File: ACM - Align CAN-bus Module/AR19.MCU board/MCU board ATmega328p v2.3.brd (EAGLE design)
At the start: 25.4 x 39 mm, 40 parts, among them IC1 ATMEGA328P-MMH, IC2 MIC5239-5.0YS_TR, IC3 MCP25625-E_ML, J1 AVR_SPI_PROG_3X2NS

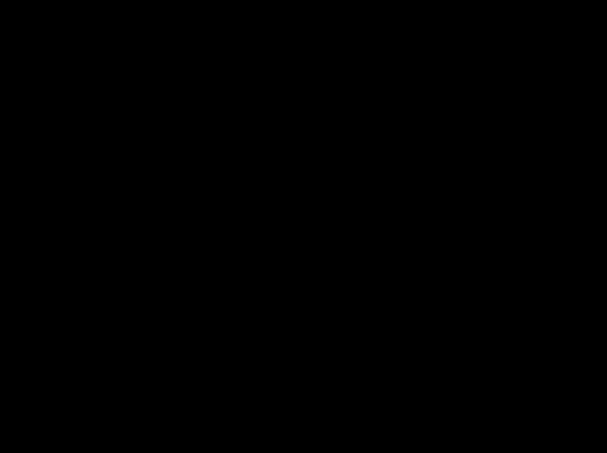
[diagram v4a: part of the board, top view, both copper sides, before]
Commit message: Added: Orange Power LED with 500ohm resistor
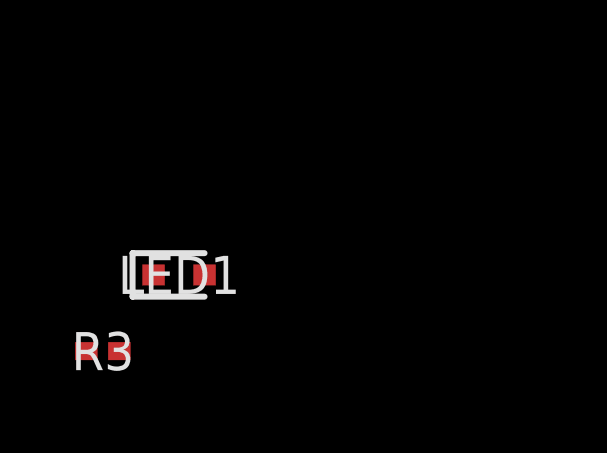
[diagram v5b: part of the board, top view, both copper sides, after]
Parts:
- added LED1: SML-A12DTT86, SML-A12DTT86:LEDC1606X125N
- added R3: 500Ohm, CRCW040295R3FKED(0402):RESC1005X40N
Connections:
- new net N$3: LED1.1, R3.1
- net GND: now also LED1.2
- net N$2: now also R3.2
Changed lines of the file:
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@@
 <attribute name="VALUE" x="10.6813" y="53.728" size="1.27" layer="27" align="center"/>
+</element>
+<element name="LED1" library="SML-A12DTT86" package="LEDC1606X125N" value="SML-A12DTT86" x="-34.29" y="-59.69" smashed="yes">
+<attribute name="ALLIED_NUMBER" value="70522054" x="-34.29" y="-59.69" size="1.778" layer="27" display="off"/>
+<attribute name="ALLIED_PRICE-STOCK" value="https://www.alliedelec.com/rohm-semiconductor-sml-a12dtt86/70522054/" x="-34.29" y="-59.69" size="1.778" layer="27" display="off"/>
+<attribute name="ARROW_PART_NUMBER" value="SML-A12DTT86" x="-34.29" y="-59.69" size="1.778" layer="27" display="off"/>
+<attribute name="ARROW_PRICE-STOCK" value="http://uk.rs-online.com/web/p/products/7008008P" x="-34.29" y="-59.69" size="1.778" layer="27" display="off"/>
+<attribute name="DESCRIPTION" value="Mini-mold side view chip LED : ROHM's chip LED lineup consists of standard type,top-view type, side-view type and reverse-mount type." x="-34.29" y="-59.69" size="1.778" layer="27" display="off"/>
+<attribute name="HEIGHT" value="1.25mm" x="-34.29" y="-59.69" size="1.778" layer="27" display="off"/>
+<attribute name="MANUFACTURER_NAME" value="ROHM Semiconductor" x="-34.29" y="-59.69" size="1.778" layer="27" display="off"/>
+<attribute name="MANUFACTURER_PART_NUMBER" value="SML-A12DTT86" x="-34.29" y="-59.69" size="1.778" layer="27" display="off"/>
+<attribute name="NAME" x="-34.29" y="-59.69" size="1.27" layer="25" align="center"/>
+<attribute name="RS_PART_NUMBER" value="7008008P" x="-34.29" y="-59.69" size="1.778" layer="27" display="off"/>
+<attribute name="RS_PRICE-STOCK" value="http://uk.rs-online.com/web/p/products/7008008P" x="-34.29" y="-59.69" size="1.778" layer="27" display="off"/>
+<attribute name="VALUE" x="-34.29" y="-59.69" size="1.27" layer="27" align="center"/>
+</element>
+<element name="R3" library="CRCW040295R3FKED(0402)" package="RESC1005X40N" value="500Ohm" x="-36.83" y="-62.23" smashed="yes">
+<attribute name="ARROW_PART_NUMBER" value="CRCW040295R3FKED" x="-36.83" y="-62.23" size="1.778" layer="27" display="off"/>
+<attribute name="ARROW_PRICE-STOCK" value="https://www.arrow.com/en/products/crcw040295r3fked/vishay" x="-36.83" y="-62.23" size="1.778" layer="27" display="off"/>
+<attribute name="DESCRIPTION" value="RESISTOR, 0402 95.3 Ohms 1% 0.063 W" x="-36.83" y="-62.23" size="1.778" layer="27" display="off"/>
+<attribute name="HEIGHT" value="0.4mm" x="-36.83" y="-62.23" size="1.778" layer="27" display="off"/>
+<attribute name="MANUFACTURER_NAME" value="Vishay" x="-36.83" y="-62.23" size="1.778" layer="27" display="off"/>
+<attribute name="MANUFACTURER_PART_NUMBER" value="CRCW040295R3FKED" x="-36.83" y="-62.23" size="1.778" layer="27" display="off"/>
+<attribute name="NAME" x="-36.83" y="-62.23" size="1.27" layer="25" align="center"/>
+<attribute name="RS_PART_NUMBER" value="" x="-36.83" y="-62.23" size="1.778" layer="27" display="off"/>
+<attribute name="RS_PRICE-STOCK" value="" x="-36.83" y="-62.23" size="1.778" layer="27" display="off"/>
+<attribute name="VALUE" x="-36.83" y="-62.23" size="1.27" layer="27" align="center"/>
 </element>
 </elements>
@@
 <contactref element="C9" pad="1"/>
 <contactref element="C10" pad="1"/>
-<wire x1="-3.305" y1="-48.26" x2="-8.385" y2="-48.26" width="0" layer="19" extent="1-1"/>
-<wire x1="-7.405" y1="-36.83" x2="-8.385" y2="-48.26" width="0" layer="19" extent="1-1"/>
-<wire x1="-7.405" y1="-31.75" x2="-7.405" y2="-36.83" width="0" layer="19" extent="1-1"/>
-<wire x1="-7.405" y1="-26.67" x2="-7.405" y2="-31.75" width="0" layer="19" extent="1-1"/>
-<wire x1="-7.405" y1="-19.05" x2="-7.405" y2="-26.67" width="0" layer="19" extent="1-1"/>
-<wire x1="-30.48" y1="-4.445" x2="-7.405" y2="-19.05" width="0" layer="19" extent="1-1"/>
-<wire x1="-9.525" y1="9.525" x2="-30.48" y2="-4.445" width="0" layer="19" extent="1-1"/>
-<wire x1="42.855" y1="-8.845" x2="-9.525" y2="9.525" width="0" layer="19" extent="1-1"/>
+<contactref element="LED1" pad="2"/>
+<wire x1="81.41" y1="-5.715" x2="95.12" y2="1.27" width="0" layer="19" extent="1-1"/>
+<wire x1="67.945" y1="-3.73" x2="81.41" y2="-5.715" width="0" layer="19" extent="1-1"/>
+<wire x1="42.855" y1="-8.845" x2="67.945" y2="-3.73" width="0" layer="19" extent="1-1"/>
 <wire x1="41.955" y1="-7.945" x2="42.855" y2="-8.845" width="0" layer="19" extent="1-1"/>
 <wire x1="40.655" y1="-7.945" x2="41.955" y2="-7.945" width="0" layer="19" extent="1-1"/>
 <wire x1="40.005" y1="-7.945" x2="40.655" y2="-7.945" width="0" layer="19" extent="1-1"/>
 <wire x1="37.155" y1="-8.845" x2="40.005" y2="-7.945" width="0" layer="19" extent="1-1"/>
-<wire x1="6.085" y1="46.875" x2="42.855" y2="-8.845" width="0" layer="19" extent="1-1"/>
-<wire x1="15.265" y1="34.29" x2="37.155" y2="-8.845" width="0" layer="19" extent="1-1"/>
-<wire x1="18.415" y1="42.545" x2="6.085" y2="46.875" width="0" layer="19" extent="1-1"/>
+<wire x1="-7.405" y1="-19.05" x2="37.155" y2="-8.845" width="0" layer="19" extent="1-1"/>
+<wire x1="-7.405" y1="-26.67" x2="-7.405" y2="-19.05" width="0" layer="19" extent="1-1"/>
+<wire x1="-7.405" y1="-31.75" x2="-7.405" y2="-26.67" width="0" layer="19" extent="1-1"/>
+<wire x1="-7.405" y1="-36.83" x2="-7.405" y2="-31.75" width="0" layer="19" extent="1-1"/>
+<wire x1="-8.385" y1="-48.26" x2="-7.405" y2="-36.83" width="0" layer="19" extent="1-1"/>
+<wire x1="-3.305" y1="-48.26" x2="-8.385" y2="-48.26" width="0" layer="19" extent="1-1"/>
+<wire x1="-30.48" y1="-4.445" x2="-7.405" y2="-19.05" width="0" layer="19" extent="1-1"/>
+<wire x1="-9.525" y1="9.525" x2="-30.48" y2="-4.445" width="0" layer="19" extent="1-1"/>
+<wire x1="-33.44" y1="-59.69" x2="-8.385" y2="-48.26" width="0" layer="19" extent="1-1"/>
+<wire x1="15.265" y1="34.29" x2="-9.525" y2="9.525" width="0" layer="19" extent="1-1"/>
+<wire x1="18.415" y1="42.545" x2="15.265" y2="34.29" width="0" layer="19" extent="1-1"/>
 <wire x1="29.13" y1="42.545" x2="18.415" y2="42.545" width="0" layer="19" extent="1-1"/>
-<wire x1="67.945" y1="-3.73" x2="37.155" y2="-8.845" width="0" layer="19" extent="1-1"/>
-<wire x1="81.41" y1="-5.715" x2="67.945" y2="-3.73" width="0" layer="19" extent="1-1"/>
-<wire x1="95.12" y1="1.27" x2="81.41" y2="-5.715" width="0" layer="19" extent="1-1"/>
+<wire x1="6.085" y1="46.875" x2="18.415" y2="42.545" width="0" layer="19" extent="1-1"/>
 </signal>
 <signal name="5V">
@@
 <contactref element="C4" pad="2"/>
 <contactref element="IC2" pad="1"/>
+<contactref element="R3" pad="2"/>
+<wire x1="10.8077" y1="35.56" x2="-36.28" y2="-62.23" width="0" layer="19" extent="1-1"/>
 <wire x1="15.265" y1="36.59" x2="10.8077" y2="35.56" width="0" layer="19" extent="1-1"/>
 <wire x1="31.83" y1="42.545" x2="15.265" y2="36.59" width="0" layer="19" extent="1-1"/>
 </signal>
+<signal name="N$3">
+<contactref element="LED1" pad="1"/>
+<contactref element="R3" pad="1"/>
+<wire x1="-35.14" y1="-59.69" x2="-37.38" y2="-62.23" width="0" layer="19" extent="1-1"/>
+</signal>
 </signals>

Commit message: -
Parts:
- moved LED1 11.7 mm to (-24.1, -54.0)
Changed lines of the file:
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@@
 <attribute name="VALUE" x="10.6813" y="53.728" size="1.27" layer="27" align="center"/>
 </element>
-<element name="LED1" library="SML-A12DTT86" package="LEDC1606X125N" value="SML-A12DTT86" x="-34.29" y="-59.69" smashed="yes">
-<attribute name="ALLIED_NUMBER" value="70522054" x="-34.29" y="-59.69" size="1.778" layer="27" display="off"/>
-<attribute name="ALLIED_PRICE-STOCK" value="https://www.alliedelec.com/rohm-semiconductor-sml-a12dtt86/70522054/" x="-34.29" y="-59.69" size="1.778" layer="27" display="off"/>
-<attribute name="ARROW_PART_NUMBER" value="SML-A12DTT86" x="-34.29" y="-59.69" size="1.778" layer="27" display="off"/>
-<attribute name="ARROW_PRICE-STOCK" value="http://uk.rs-online.com/web/p/products/7008008P" x="-34.29" y="-59.69" size="1.778" layer="27" display="off"/>
-<attribute name="DESCRIPTION" value="Mini-mold side view chip LED : ROHM's chip LED lineup consists of standard type,top-view type, side-view type and reverse-mount type." x="-34.29" y="-59.69" size="1.778" layer="27" display="off"/>
-<attribute name="HEIGHT" value="1.25mm" x="-34.29" y="-59.69" size="1.778" layer="27" display="off"/>
-<attribute name="MANUFACTURER_NAME" value="ROHM Semiconductor" x="-34.29" y="-59.69" size="1.778" layer="27" display="off"/>
-<attribute name="MANUFACTURER_PART_NUMBER" value="SML-A12DTT86" x="-34.29" y="-59.69" size="1.778" layer="27" display="off"/>
-<attribute name="NAME" x="-34.29" y="-59.69" size="1.27" layer="25" align="center"/>
-<attribute name="RS_PART_NUMBER" value="7008008P" x="-34.29" y="-59.69" size="1.778" layer="27" display="off"/>
-<attribute name="RS_PRICE-STOCK" value="http://uk.rs-online.com/web/p/products/7008008P" x="-34.29" y="-59.69" size="1.778" layer="27" display="off"/>
-<attribute name="VALUE" x="-34.29" y="-59.69" size="1.27" layer="27" align="center"/>
+<element name="LED1" library="SML-A12DTT86" package="LEDC1606X125N" value="SML-A12DTT86" x="-24.13" y="-53.975" smashed="yes">
+<attribute name="ALLIED_NUMBER" value="70522054" x="-24.13" y="-53.975" size="1.778" layer="27" display="off"/>
+<attribute name="ALLIED_PRICE-STOCK" value="https://www.alliedelec.com/rohm-semiconductor-sml-a12dtt86/70522054/" x="-24.13" y="-53.975" size="1.778" layer="27" display="off"/>
+<attribute name="ARROW_PART_NUMBER" value="SML-A12DTT86" x="-24.13" y="-53.975" size="1.778" layer="27" display="off"/>
+<attribute name="ARROW_PRICE-STOCK" value="http://uk.rs-online.com/web/p/products/7008008P" x="-24.13" y="-53.975" size="1.778" layer="27" display="off"/>
+<attribute name="DESCRIPTION" value="Mini-mold side view chip LED : ROHM's chip LED lineup consists of standard type,top-view type, side-view type and reverse-mount type." x="-24.13" y="-53.975" size="1.778" layer="27" display="off"/>
+<attribute name="HEIGHT" value="1.25mm" x="-24.13" y="-53.975" size="1.778" layer="27" display="off"/>
+<attribute name="MANUFACTURER_NAME" value="ROHM Semiconductor" x="-24.13" y="-53.975" size="1.778" layer="27" display="off"/>
+<attribute name="MANUFACTURER_PART_NUMBER" value="SML-A12DTT86" x="-24.13" y="-53.975" size="1.778" layer="27" display="off"/>
+<attribute name="NAME" x="-26.035" y="-52.07" size="1.27" layer="25" align="center"/>
+<attribute name="RS_PART_NUMBER" value="7008008P" x="-24.13" y="-53.975" size="1.778" layer="27" display="off"/>
+<attribute name="RS_PRICE-STOCK" value="http://uk.rs-online.com/web/p/products/7008008P" x="-24.13" y="-53.975" size="1.778" layer="27" display="off"/>
+<attribute name="VALUE" x="-23.495" y="-50.165" size="1.27" layer="27" align="center"/>
 </element>
 <element name="R3" library="CRCW040295R3FKED(0402)" package="RESC1005X40N" value="500Ohm" x="-36.83" y="-62.23" smashed="yes">
@@
 <wire x1="-30.48" y1="-4.445" x2="-7.405" y2="-19.05" width="0" layer="19" extent="1-1"/>
 <wire x1="-9.525" y1="9.525" x2="-30.48" y2="-4.445" width="0" layer="19" extent="1-1"/>
-<wire x1="-33.44" y1="-59.69" x2="-8.385" y2="-48.26" width="0" layer="19" extent="1-1"/>
+<wire x1="-23.28" y1="-53.975" x2="-8.385" y2="-48.26" width="0" layer="19" extent="1-1"/>
 <wire x1="15.265" y1="34.29" x2="-9.525" y2="9.525" width="0" layer="19" extent="1-1"/>
 <wire x1="18.415" y1="42.545" x2="15.265" y2="34.29" width="0" layer="19" extent="1-1"/>
@@
 <contactref element="LED1" pad="1"/>
 <contactref element="R3" pad="1"/>
-<wire x1="-35.14" y1="-59.69" x2="-37.38" y2="-62.23" width="0" layer="19" extent="1-1"/>
+<wire x1="-24.98" y1="-53.975" x2="-37.38" y2="-62.23" width="0" layer="19" extent="1-1"/>
 </signal>
 </signals>

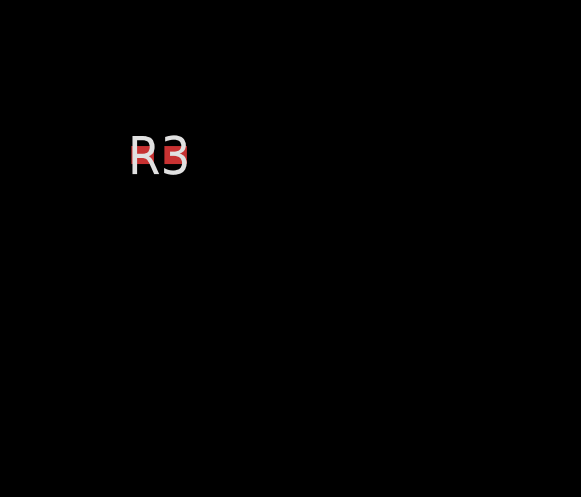
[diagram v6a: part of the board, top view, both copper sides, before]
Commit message: Added: Datasheets and capacitors to ATMEGA328p
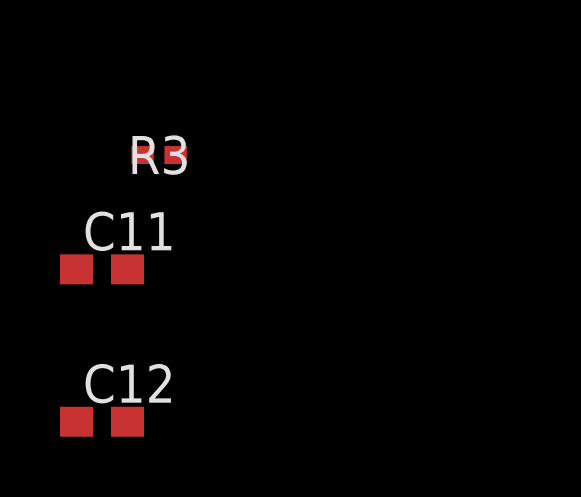
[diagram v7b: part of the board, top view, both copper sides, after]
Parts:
- added C11, C12: 0.1uF, eagle-ltspice:C0603
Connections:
- new net N$4: IC1.29
- net 5V: now also C11.1, C12.1, IC1.16
- net GND: now also C11.2, C12.2, IC1.18, IC1.4
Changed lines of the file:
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@@
 <attribute name="VALUE" x="-36.83" y="-62.23" size="1.27" layer="27" align="center"/>
+</element>
+<element name="C11" library="eagle-ltspice" library_urn="urn:adsk.eagle:library:217" package="C0603" package3d_urn="urn:adsk.eagle:package:13262/1" value="0.1uF" x="-38.735" y="-66.04" smashed="yes">
+<attribute name="NAME" x="-39.37" y="-65.405" size="1.27" layer="25"/>
+<attribute name="SPICEMODEL" value="NONE" x="-38.735" y="-66.04" size="1.778" layer="27" display="off"/>
+<attribute name="SPICEPREFIX" value="C" x="-38.735" y="-66.04" size="1.778" layer="27" display="off"/>
+<attribute name="VALUE" x="-39.37" y="-67.945" size="1.27" layer="27"/>
+</element>
+<element name="C12" library="eagle-ltspice" library_urn="urn:adsk.eagle:library:217" package="C0603" package3d_urn="urn:adsk.eagle:package:13262/1" value="0.1uF" x="-38.735" y="-71.12" smashed="yes">
+<attribute name="NAME" x="-39.37" y="-70.485" size="1.27" layer="25"/>
+<attribute name="SPICEMODEL" value="NONE" x="-38.735" y="-71.12" size="1.778" layer="27" display="off"/>
+<attribute name="SPICEPREFIX" value="C" x="-38.735" y="-71.12" size="1.778" layer="27" display="off"/>
+<attribute name="VALUE" x="-39.37" y="-73.025" size="1.27" layer="27"/>
 </element>
 </elements>
@@
 <contactref element="C4" pad="1"/>
 <contactref element="DOTSTAR" pad="3"/>
-<contactref element="IC3" pad="22"/>
 <contactref element="C5" pad="2"/>
 <contactref element="IC3" pad="18"/>
@@
 <contactref element="C10" pad="1"/>
 <contactref element="LED1" pad="2"/>
-<wire x1="81.41" y1="-5.715" x2="95.12" y2="1.27" width="0" layer="19" extent="1-1"/>
-<wire x1="67.945" y1="-3.73" x2="81.41" y2="-5.715" width="0" layer="19" extent="1-1"/>
-<wire x1="42.855" y1="-8.845" x2="67.945" y2="-3.73" width="0" layer="19" extent="1-1"/>
-<wire x1="41.955" y1="-7.945" x2="42.855" y2="-8.845" width="0" layer="19" extent="1-1"/>
-<wire x1="40.655" y1="-7.945" x2="41.955" y2="-7.945" width="0" layer="19" extent="1-1"/>
-<wire x1="40.005" y1="-7.945" x2="40.655" y2="-7.945" width="0" layer="19" extent="1-1"/>
-<wire x1="37.155" y1="-8.845" x2="40.005" y2="-7.945" width="0" layer="19" extent="1-1"/>
-<wire x1="-7.405" y1="-19.05" x2="37.155" y2="-8.845" width="0" layer="19" extent="1-1"/>
-<wire x1="-7.405" y1="-26.67" x2="-7.405" y2="-19.05" width="0" layer="19" extent="1-1"/>
-<wire x1="-7.405" y1="-31.75" x2="-7.405" y2="-26.67" width="0" layer="19" extent="1-1"/>
-<wire x1="-7.405" y1="-36.83" x2="-7.405" y2="-31.75" width="0" layer="19" extent="1-1"/>
-<wire x1="-8.385" y1="-48.26" x2="-7.405" y2="-36.83" width="0" layer="19" extent="1-1"/>
+<contactref element="IC3" pad="22"/>
+<contactref element="IC1" pad="4"/>
+<contactref element="C11" pad="2"/>
+<contactref element="C12" pad="2"/>
+<contactref element="IC1" pad="18"/>
+<wire x1="-37.885" y1="-66.04" x2="-37.885" y2="-71.12" width="0" layer="19" extent="1-1"/>
+<wire x1="-23.28" y1="-53.975" x2="-37.885" y2="-66.04" width="0" layer="19" extent="1-1"/>
+<wire x1="-8.385" y1="-48.26" x2="-23.28" y2="-53.975" width="0" layer="19" extent="1-1"/>
 <wire x1="-3.305" y1="-48.26" x2="-8.385" y2="-48.26" width="0" layer="19" extent="1-1"/>
+<wire x1="-7.405" y1="-36.83" x2="-8.385" y2="-48.26" width="0" layer="19" extent="1-1"/>
+<wire x1="-7.405" y1="-31.75" x2="-7.405" y2="-36.83" width="0" layer="19" extent="1-1"/>
+<wire x1="-7.405" y1="-26.67" x2="-7.405" y2="-31.75" width="0" layer="19" extent="1-1"/>
+<wire x1="-7.405" y1="-19.05" x2="-7.405" y2="-26.67" width="0" layer="19" extent="1-1"/>
 <wire x1="-30.48" y1="-4.445" x2="-7.405" y2="-19.05" width="0" layer="19" extent="1-1"/>
 <wire x1="-9.525" y1="9.525" x2="-30.48" y2="-4.445" width="0" layer="19" extent="1-1"/>
-<wire x1="-23.28" y1="-53.975" x2="-8.385" y2="-48.26" width="0" layer="19" extent="1-1"/>
-<wire x1="15.265" y1="34.29" x2="-9.525" y2="9.525" width="0" layer="19" extent="1-1"/>
+<wire x1="6.985" y1="23.985" x2="-9.525" y2="9.525" width="0" layer="19" extent="1-1"/>
+<wire x1="6.985" y1="28.085" x2="6.985" y2="23.985" width="0" layer="19" extent="1-1"/>
+<wire x1="15.265" y1="34.29" x2="6.985" y2="28.085" width="0" layer="19" extent="1-1"/>
 <wire x1="18.415" y1="42.545" x2="15.265" y2="34.29" width="0" layer="19" extent="1-1"/>
 <wire x1="29.13" y1="42.545" x2="18.415" y2="42.545" width="0" layer="19" extent="1-1"/>
 <wire x1="6.085" y1="46.875" x2="18.415" y2="42.545" width="0" layer="19" extent="1-1"/>
+<wire x1="37.155" y1="-8.845" x2="6.985" y2="23.985" width="0" layer="19" extent="1-1"/>
+<wire x1="40.005" y1="-7.945" x2="37.155" y2="-8.845" width="0" layer="19" extent="1-1"/>
+<wire x1="40.655" y1="-7.945" x2="40.005" y2="-7.945" width="0" layer="19" extent="1-1"/>
+<wire x1="41.955" y1="-7.945" x2="40.655" y2="-7.945" width="0" layer="19" extent="1-1"/>
+<wire x1="42.855" y1="-8.845" x2="41.955" y2="-7.945" width="0" layer="19" extent="1-1"/>
+<wire x1="67.945" y1="-3.73" x2="42.855" y2="-8.845" width="0" layer="19" extent="1-1"/>
+<wire x1="81.41" y1="-5.715" x2="67.945" y2="-3.73" width="0" layer="19" extent="1-1"/>
+<wire x1="95.12" y1="1.27" x2="81.41" y2="-5.715" width="0" layer="19" extent="1-1"/>
 </signal>
 <signal name="5V">
@@
 <contactref element="C8" pad="1"/>
 <contactref element="IC3" pad="3"/>
+<contactref element="C11" pad="1"/>
+<contactref element="C12" pad="1"/>
+<contactref element="IC1" pad="16"/>
+<wire x1="-39.585" y1="-66.04" x2="-39.585" y2="-71.12" width="0" layer="19" extent="1-1"/>
+<wire x1="-9.105" y1="-36.83" x2="-39.585" y2="-66.04" width="0" layer="19" extent="1-1"/>
 <wire x1="-9.105" y1="-31.75" x2="-9.105" y2="-36.83" width="0" layer="19" extent="1-1"/>
 <wire x1="-9.105" y1="-26.67" x2="-9.105" y2="-31.75" width="0" layer="19" extent="1-1"/>
 <wire x1="-5.303" y1="-22.86" x2="-9.105" y2="-26.67" width="0" layer="19" extent="1-1"/>
 <wire x1="-9.525" y1="4.445" x2="-5.303" y2="-22.86" width="0" layer="19" extent="1-1"/>
-<wire x1="-9.525" y1="44.673" x2="-9.525" y2="4.445" width="0" layer="19" extent="1-1"/>
-<wire x1="7.885" y1="46.875" x2="-9.525" y2="44.673" width="0" layer="19" extent="1-1"/>
-<wire x1="42.855" y1="-10.795" x2="7.885" y2="46.875" width="0" layer="19" extent="1-1"/>
+<wire x1="6.535" y1="23.985" x2="-9.525" y2="4.445" width="0" layer="19" extent="1-1"/>
+<wire x1="7.885" y1="28.085" x2="6.535" y2="23.985" width="0" layer="19" extent="1-1"/>
+<wire x1="15.265" y1="31.99" x2="7.885" y2="28.085" width="0" layer="19" extent="1-1"/>
+<wire x1="7.885" y1="46.875" x2="15.265" y2="31.99" width="0" layer="19" extent="1-1"/>
+<wire x1="-9.525" y1="44.673" x2="7.885" y2="46.875" width="0" layer="19" extent="1-1"/>
+<wire x1="39.355" y1="-13.645" x2="-5.303" y2="-22.86" width="0" layer="19" extent="1-1"/>
+<wire x1="42.855" y1="-10.795" x2="39.355" y2="-13.645" width="0" layer="19" extent="1-1"/>
 <wire x1="39.355" y1="-7.945" x2="42.855" y2="-10.795" width="0" layer="19" extent="1-1"/>
-<wire x1="6.535" y1="23.985" x2="39.355" y2="-7.945" width="0" layer="19" extent="1-1"/>
-<wire x1="39.355" y1="-13.645" x2="42.855" y2="-10.795" width="0" layer="19" extent="1-1"/>
-<wire x1="15.265" y1="31.99" x2="39.355" y2="-13.645" width="0" layer="19" extent="1-1"/>
-<wire x1="67.945" y1="-6.43" x2="39.355" y2="-7.945" width="0" layer="19" extent="1-1"/>
+<wire x1="67.945" y1="-6.43" x2="42.855" y2="-10.795" width="0" layer="19" extent="1-1"/>
 </signal>
 <signal name="MOSI">
@@
 <wire x1="-24.98" y1="-53.975" x2="-37.38" y2="-62.23" width="0" layer="19" extent="1-1"/>
 </signal>
+<signal name="N$4">
+<contactref element="IC1" pad="29"/>
+</signal>
 </signals>
